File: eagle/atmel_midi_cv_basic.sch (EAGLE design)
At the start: 46 parts, among them IC1 TL072P, IC2 TL072P, U1 ATMEGA328P_PDIP

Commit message: possible route
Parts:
- renumbered R6 to SCALE_TRIM
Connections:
- removed net GND: AMT.A, C1.1, C2.1, C3.2, C4.2, C5.-, C6.2, C7.2, C8.2, GATE.RING, IC1P.V-, IC2P.V-, MIDI_CH.E, OK1.GND, PITCH.RING, PWM_OUT.RING, PWR1.GND, R13.2, R25.1, R8.1, RST2.P, SCALE_TRIM.E, U$4.AVSS, U$4.~LDAC, U1.GND@1, U1.GND@2, VEL.RING
- new net N$29: AMT.A, C1.1, C2.1, C3.2, C4.2, C5.-, C6.2, C7.2, C8.2, GATE.RING, IC1P.V-, IC2P.V-, MIDI_CH.A, OK1.GND, PITCH.RING, PWM_OUT.RING, PWR1.GND, R13.2, R25.1, R8.1, RST2.P, SCALE_TRIM.E, U$4.AVSS, U$4.~LDAC, U1.GND@1, U1.GND@2, VEL.RING
- net +5V: now also MIDI_CH.E; no longer MIDI_CH.A
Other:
- moved on the sheet: MIDI_CH
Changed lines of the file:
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@@
 <part name="GND2" library="supply1" deviceset="GND" device=""/>
 <part name="R5" library="rcl" deviceset="R-US_" device="0207/10" value="3k3"/>
-<part name="R6" library="pot" deviceset="TRIM_US-" device="B64W" value="10k"/>
+<part name="SCALE_TRIM" library="pot" deviceset="TRIM_US-" device="B64W" value="10k"/>
 <part name="GND4" library="supply1" deviceset="GND" device=""/>
 <part name="R7" library="rcl" deviceset="R-US_" device="0207/10" value="5k"/>
@@
 <instance part="GND2" gate="1" x="40.64" y="91.44"/>
 <instance part="R5" gate="G$1" x="119.38" y="116.84"/>
-<instance part="R6" gate="G$1" x="121.92" y="104.14" rot="MR180"/>
+<instance part="SCALE_TRIM" gate="G$1" x="121.92" y="104.14" rot="MR180"/>
 <instance part="GND4" gate="1" x="121.92" y="91.44"/>
 <instance part="R7" gate="G$1" x="139.7" y="96.52"/>
@@
 <instance part="GATE" gate="G$1" x="58.42" y="-7.62" rot="R180"/>
 <instance part="GND3" gate="1" x="50.8" y="-30.48"/>
-<instance part="MIDI_CH" gate="G$1" x="55.88" y="73.66" rot="R180"/>
+<instance part="MIDI_CH" gate="G$1" x="55.88" y="73.66" rot="MR0"/>
 <instance part="P+3" gate="1" x="55.88" y="86.36"/>
 <instance part="GND7" gate="1" x="55.88" y="60.96"/>
@@
 </segment>
 <segment>
-<pinref part="MIDI_CH" gate="G$1" pin="A"/>
-<pinref part="P+3" gate="1" pin="+5V"/>
-<wire x1="55.88" y1="83.82" x2="55.88" y2="81.28" width="0.1524" layer="91"/>
-</segment>
-<segment>
 <pinref part="P+7" gate="1" pin="+5V"/>
 <wire x1="116.84" y1="10.16" x2="116.84" y2="-10.16" width="0.1524" layer="91"/>
@@
 <wire x1="116.84" y1="-10.16" x2="114.3" y2="-10.16" width="0.1524" layer="91"/>
 </segment>
-</net>
-<net name="GND" class="0">
+<segment>
+<pinref part="P+3" gate="1" pin="+5V"/>
+<pinref part="MIDI_CH" gate="G$1" pin="E"/>
+<wire x1="55.88" y1="81.28" x2="55.88" y2="83.82" width="0.1524" layer="91"/>
+</segment>
+</net>
+<net name="N$29" class="0">
 <segment>
 <pinref part="GND2" gate="1" pin="GND"/>
@@
 </segment>
 <segment>
-<pinref part="MIDI_CH" gate="G$1" pin="E"/>
-<pinref part="GND7" gate="1" pin="GND"/>
-<wire x1="55.88" y1="63.5" x2="55.88" y2="66.04" width="0.1524" layer="91"/>
-</segment>
-<segment>
 <pinref part="GND8" gate="1" pin="GND"/>
 <wire x1="78.74" y1="50.8" x2="86.36" y2="50.8" width="0.1524" layer="91"/>
@@
 <segment>
 <pinref part="GND4" gate="1" pin="GND"/>
-<pinref part="R6" gate="G$1" pin="E"/>
+<pinref part="SCALE_TRIM" gate="G$1" pin="E"/>
 <wire x1="121.92" y1="96.52" x2="121.92" y2="93.98" width="0.1524" layer="91"/>
 </segment>
@@
 <wire x1="99.06" y1="12.7" x2="93.98" y2="12.7" width="0.1524" layer="91"/>
 <junction x="93.98" y="12.7"/>
+</segment>
+<segment>
+<pinref part="GND7" gate="1" pin="GND"/>
+<pinref part="MIDI_CH" gate="G$1" pin="A"/>
+<wire x1="55.88" y1="66.04" x2="55.88" y2="63.5" width="0.1524" layer="91"/>
 </segment>
 </net>
@@
 <net name="N$12" class="0">
 <segment>
-<pinref part="R6" gate="G$1" pin="S"/>
+<pinref part="SCALE_TRIM" gate="G$1" pin="S"/>
 <wire x1="127" y1="104.14" x2="129.54" y2="104.14" width="0.1524" layer="91"/>
 <wire x1="129.54" y1="104.14" x2="129.54" y2="111.76" width="0.1524" layer="91"/>
@@
 <net name="N$22" class="0">
 <segment>
-<pinref part="U1" gate="G$1" pin="PD3(INT1)"/>
-<wire x1="43.18" y1="43.18" x2="55.88" y2="43.18" width="0.1524" layer="91"/>
 <wire x1="55.88" y1="43.18" x2="55.88" y2="7.62" width="0.1524" layer="91"/>
 <wire x1="55.88" y1="7.62" x2="-2.54" y2="7.62" width="0.1524" layer="91"/>
@@
 <wire x1="-2.54" y1="7.62" x2="-2.54" y2="0" width="0.1524" layer="91"/>
 <pinref part="IC2" gate="B" pin="+IN"/>
+<pinref part="U1" gate="G$1" pin="PD3(INT1)"/>
+<wire x1="55.88" y1="43.18" x2="43.18" y2="43.18" width="0.1524" layer="91"/>
 </segment>
 </net>
@@
 <wire x1="78.74" y1="33.02" x2="78.74" y2="40.64" width="0.1524" layer="91"/>
 <pinref part="U1" gate="G$1" pin="PD4(XCK/T0)"/>
-<wire x1="78.74" y1="40.64" x2="43.18" y2="40.64" width="0.1524" layer="91"/>
-</segment>
-</net>
+<wire x1="43.18" y1="40.64" x2="78.74" y2="40.64" width="0.1524" layer="91"/>
+</segment>
+</net>

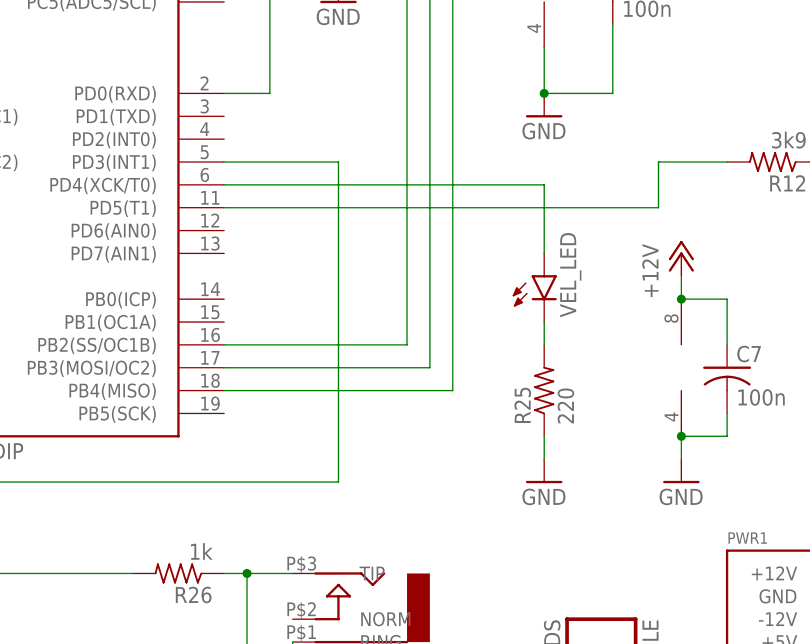
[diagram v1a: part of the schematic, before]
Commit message: fixed led output to pwm pin and schematic consistent
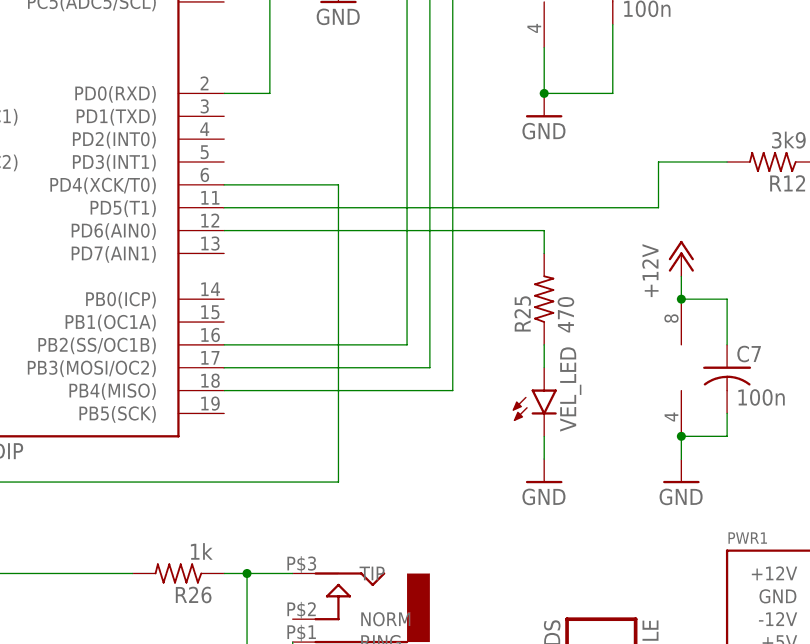
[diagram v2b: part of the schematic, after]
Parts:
- R25: value 220 -> 470
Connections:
- new net GND: VEL_LED.C
- net N$18: now also R25.1, VEL_LED.A; no longer R25.2, VEL_LED.C
- net N$20: now also R25.2, U1.PD6(AIN0); no longer U1.PD4(XCK/T0), VEL_LED.A
- net N$22: now also U1.PD4(XCK/T0); no longer U1.PD3(INT1)
- net N$29: no longer R25.1
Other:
- moved on the sheet: R25, VEL_LED
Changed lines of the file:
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@@
 <part name="GND9" library="supply1" deviceset="GND" device=""/>
 <part name="R24" library="rcl" deviceset="R-US_" device="0207/10" value="1M"/>
-<part name="R25" library="rcl" deviceset="R-US_" device="0207/10" value="220"/>
+<part name="R25" library="rcl" deviceset="R-US_" device="0207/10" value="470"/>
 <part name="AMT" library="pot" deviceset="3RP/1610N" device="" value="100k"/>
 <part name="GND19" library="supply1" deviceset="GND" device=""/>
@@
 <part name="GND11" library="supply1" deviceset="GND" device=""/>
 <part name="GND15" library="supply1" deviceset="GND" device=""/>
-<part name="GND13" library="supply1" deviceset="GND" device=""/>
 <part name="R4" library="rcl" deviceset="R-US_" device="0207/10" value="1k"/>
 <part name="PWM_OUT" library="erthenvar" deviceset="AUDIO-JACK" device=""/>
@@
 <part name="GATE_BUS_ENABLE" library="SparkFun-Connectors" deviceset="M02" device="LOCK_LONGPADS"/>
 <part name="CV_BUS_ENABLE" library="SparkFun-Connectors" deviceset="M02" device="LOCK_LONGPADS"/>
+<part name="GND13" library="supply1" deviceset="GND" device=""/>
 </parts>
 <sheets>
@@
 <instance part="GND9" gate="1" x="20.32" y="81.28"/>
 <instance part="R24" gate="G$1" x="-20.32" y="45.72" rot="R90"/>
-<instance part="R25" gate="G$1" x="78.74" y="17.78" rot="R90"/>
+<instance part="R25" gate="G$1" x="78.74" y="27.94" rot="R90"/>
 <instance part="AMT" gate="G$1" x="152.4" y="73.66"/>
 <instance part="GND19" gate="1" x="152.4" y="60.96"/>
-<instance part="VEL_LED" gate="G$1" x="78.74" y="30.48"/>
+<instance part="VEL_LED" gate="G$1" x="78.74" y="17.78"/>
 <instance part="R9" gate="G$1" x="5.08" y="-12.7" rot="R180"/>
 <instance part="R26" gate="G$1" x="38.1" y="-2.54" rot="R180"/>
@@
 <instance part="GND11" gate="1" x="160.02" y="60.96"/>
 <instance part="GND15" gate="1" x="167.64" y="101.6"/>
-<instance part="GND13" gate="1" x="78.74" y="7.62"/>
 <instance part="R4" gate="G$1" x="152.4" y="40.64"/>
 <instance part="PWM_OUT" gate="G$1" x="167.64" y="35.56" rot="R180"/>
@@
 <instance part="GATE_BUS_ENABLE" gate="G$1" x="83.82" y="-10.16" rot="R270"/>
 <instance part="CV_BUS_ENABLE" gate="G$1" x="170.18" y="15.24"/>
+<instance part="GND13" gate="1" x="78.74" y="7.62"/>
 </instances>
 <busses>
@@
 </segment>
 <segment>
-<pinref part="R25" gate="G$1" pin="1"/>
-<pinref part="GND13" gate="1" pin="GND"/>
-<wire x1="78.74" y1="10.16" x2="78.74" y2="12.7" width="0.1524" layer="91"/>
-</segment>
-<segment>
 <pinref part="PWM_OUT" gate="G$1" pin="RING"/>
 <pinref part="GND16" gate="1" pin="GND"/>
@@
 <net name="N$22" class="0">
 <segment>
-<wire x1="55.88" y1="43.18" x2="55.88" y2="7.62" width="0.1524" layer="91"/>
+<wire x1="55.88" y1="40.64" x2="55.88" y2="7.62" width="0.1524" layer="91"/>
 <wire x1="55.88" y1="7.62" x2="-2.54" y2="7.62" width="0.1524" layer="91"/>
 <wire x1="-2.54" y1="0" x2="0" y2="0" width="0.1524" layer="91"/>
 <wire x1="-2.54" y1="7.62" x2="-2.54" y2="0" width="0.1524" layer="91"/>
 <pinref part="IC2" gate="B" pin="+IN"/>
-<pinref part="U1" gate="G$1" pin="PD3(INT1)"/>
-<wire x1="55.88" y1="43.18" x2="43.18" y2="43.18" width="0.1524" layer="91"/>
+<wire x1="55.88" y1="40.64" x2="43.18" y2="40.64" width="0.1524" layer="91"/>
+<pinref part="U1" gate="G$1" pin="PD4(XCK/T0)"/>
 </segment>
 </net>
@@
 <net name="N$20" class="0">
 <segment>
-<pinref part="VEL_LED" gate="G$1" pin="A"/>
-<wire x1="78.74" y1="33.02" x2="78.74" y2="40.64" width="0.1524" layer="91"/>
-<pinref part="U1" gate="G$1" pin="PD4(XCK/T0)"/>
-<wire x1="43.18" y1="40.64" x2="78.74" y2="40.64" width="0.1524" layer="91"/>
+<wire x1="78.74" y1="35.56" x2="43.18" y2="35.56" width="0.1524" layer="91"/>
+<pinref part="U1" gate="G$1" pin="PD6(AIN0)"/>
+<pinref part="R25" gate="G$1" pin="2"/>
+<wire x1="78.74" y1="33.02" x2="78.74" y2="35.56" width="0.1524" layer="91"/>
 </segment>
 </net>
@@
 </segment>
 </net>
-<net name="N$18" class="0">
-<segment>
-<pinref part="VEL_LED" gate="G$1" pin="C"/>
-<pinref part="R25" gate="G$1" pin="2"/>
-<wire x1="78.74" y1="22.86" x2="78.74" y2="25.4" width="0.1524" layer="91"/>
-</segment>
-</net>
 <net name="N$10" class="0">
 <segment>
@@
 </segment>
 </net>
+<net name="N$18" class="0">
+<segment>
+<pinref part="VEL_LED" gate="G$1" pin="A"/>
+<pinref part="R25" gate="G$1" pin="1"/>
+<wire x1="78.74" y1="22.86" x2="78.74" y2="20.32" width="0.1524" layer="91"/>
+</segment>
+</net>
+<net name="GND" class="0">
+<segment>
+<pinref part="VEL_LED" gate="G$1" pin="C"/>
+<pinref part="GND13" gate="1" pin="GND"/>
+<wire x1="78.74" y1="10.16" x2="78.74" y2="12.7" width="0.1524" layer="91"/>
+</segment>
+</net>

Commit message: cleaned up some routes
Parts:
- R1, R10, R11, R12, R13, R2, R24, R25, R26, R3, R4, R5, R7, R8, R9: device rcl:R-US_0207/10 -> rcl:R-US_0207/7

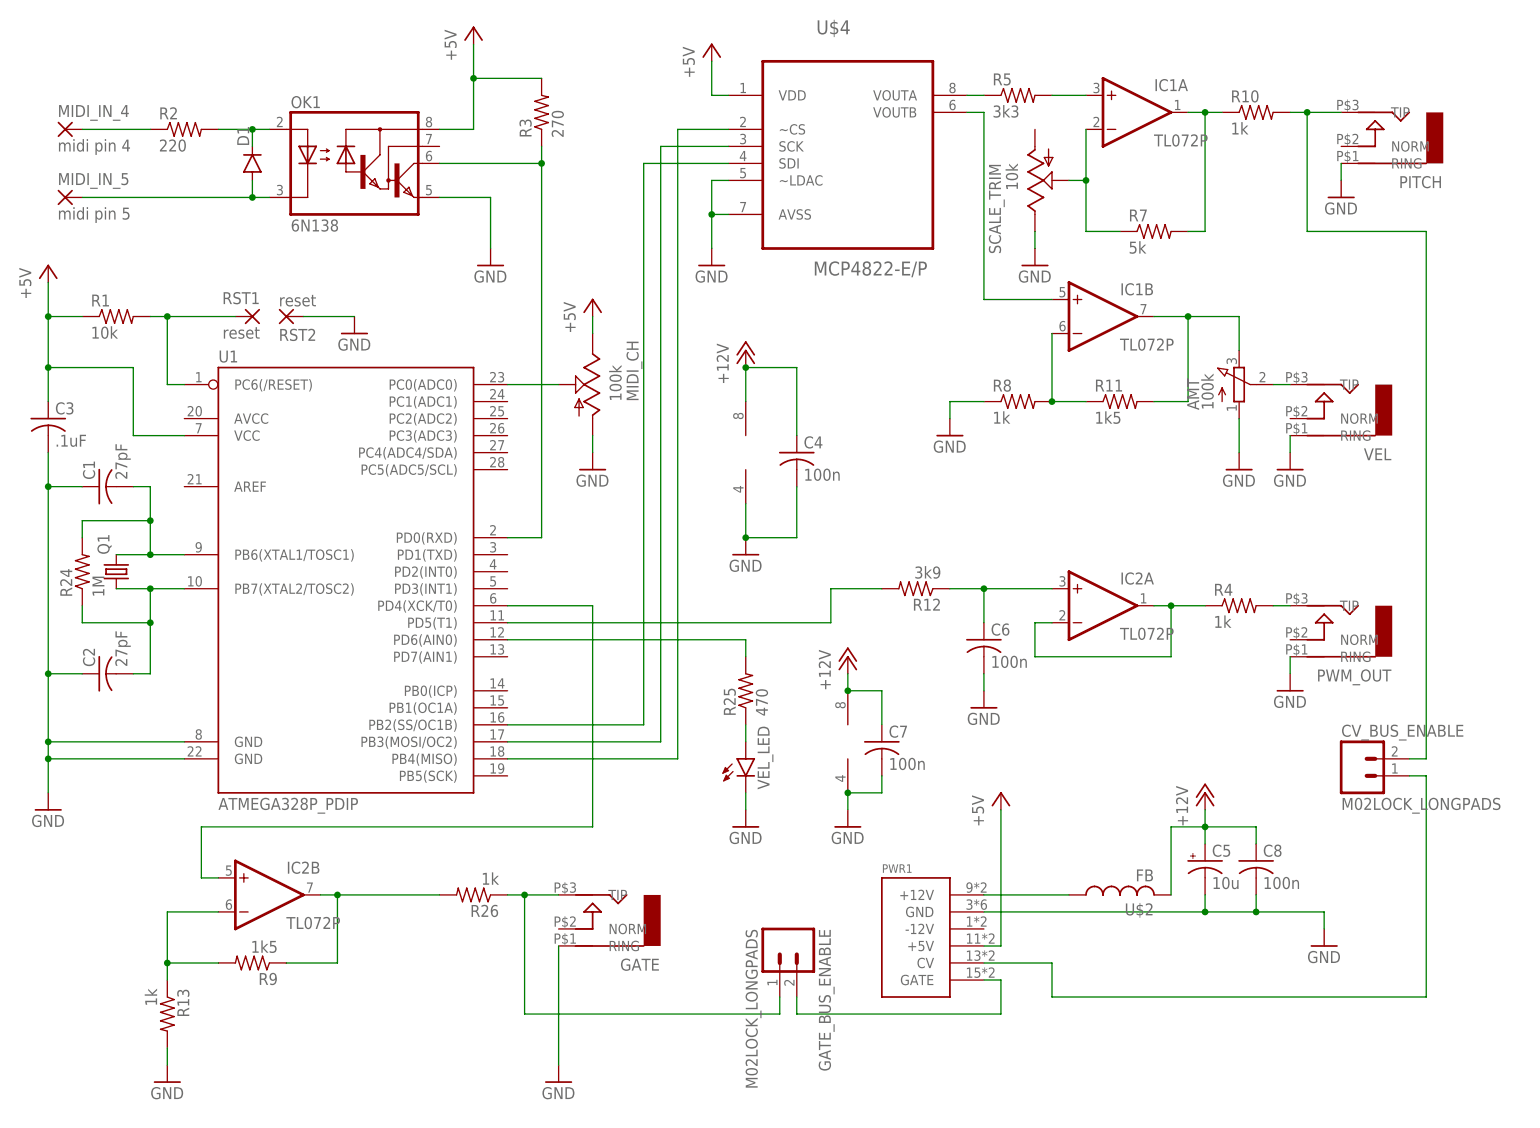
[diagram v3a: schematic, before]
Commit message: corrected wrong gate pin and tl072 back to bipolar to prevent locking
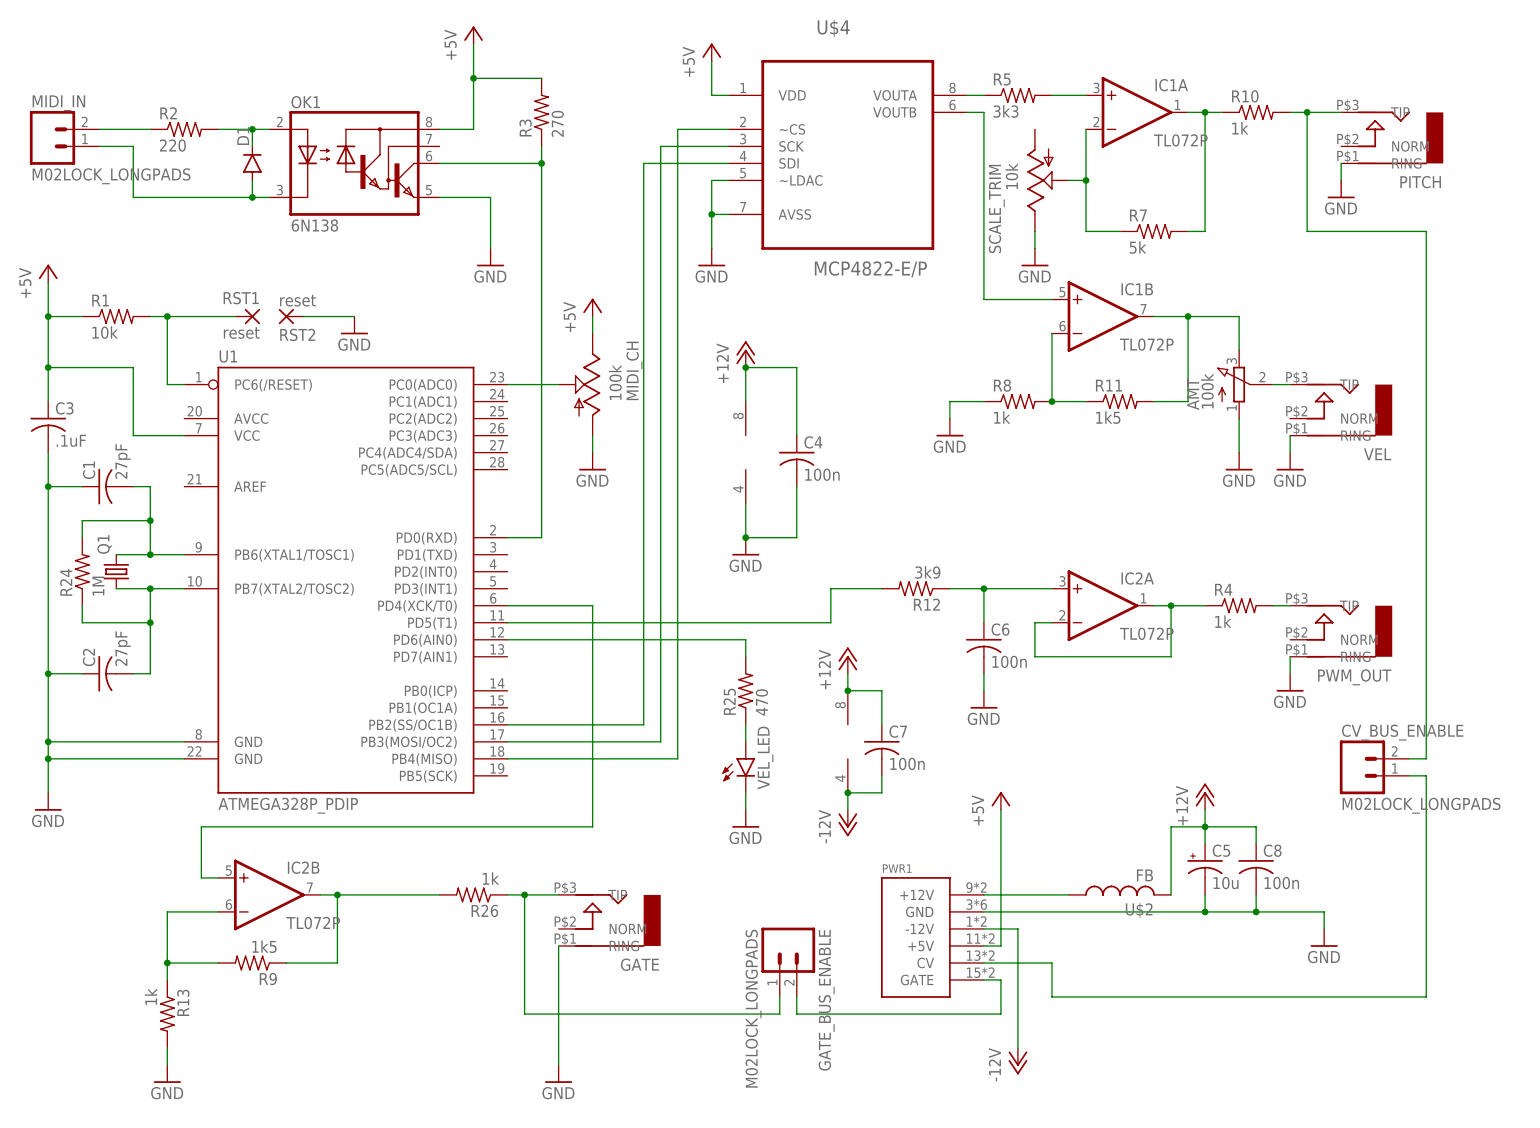
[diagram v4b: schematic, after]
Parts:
- removed MIDI_IN_4: midi pin 4, wirepad:2,54/0,9
- removed MIDI_IN_5: midi pin 5, wirepad:2,54/0,9
- added MIDI_IN: M02LOCK_LONGPADS, SparkFun-Connectors:M02LOCK_LONGPADS
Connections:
- new net -12V: C7.2, IC2P.V-, PWR1.-12V
- net N$29: no longer C7.2, IC2P.V-
- net N$3: now also MIDI_IN.1; no longer MIDI_IN_5.P
- net N$8: now also MIDI_IN.2; no longer MIDI_IN_4.P
